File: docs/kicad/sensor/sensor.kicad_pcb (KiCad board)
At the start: 2 copper layers, 30 x 26 mm, 6 parts, among them J1 G 5 L D

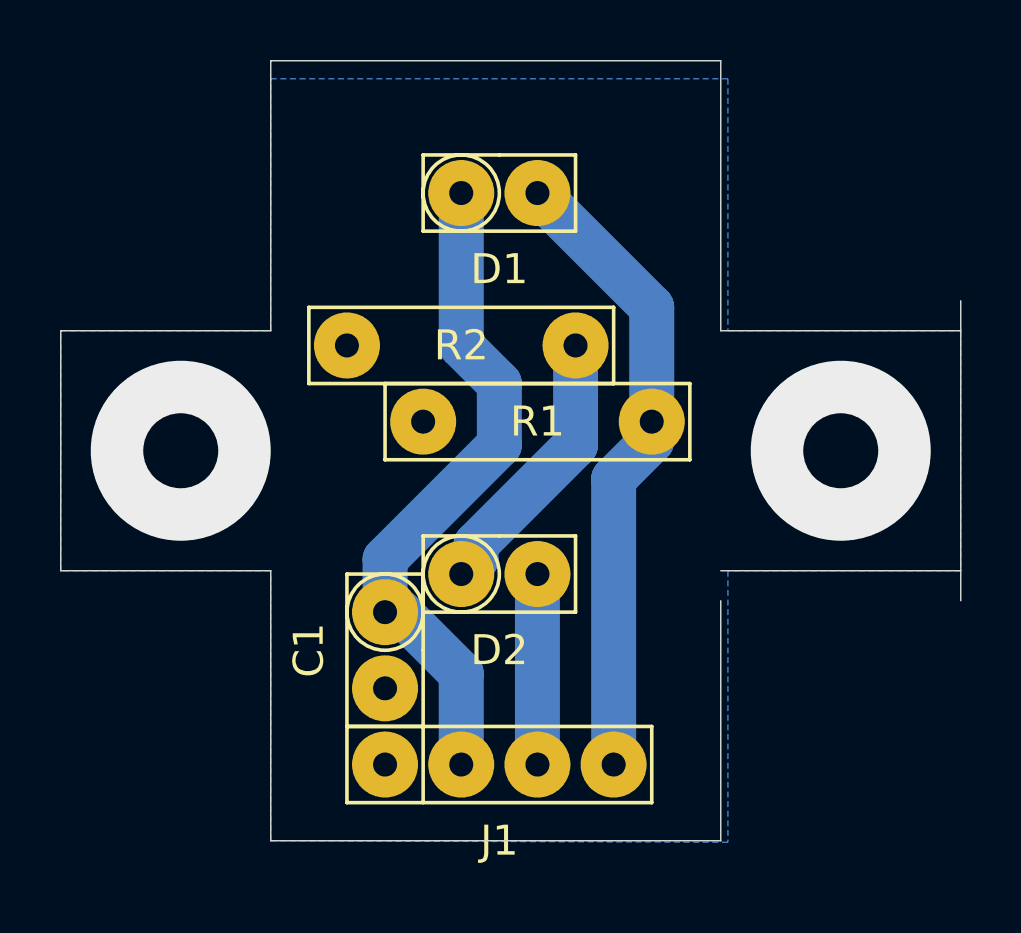
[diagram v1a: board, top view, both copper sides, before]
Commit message: SIMPLIFY: got rid of buttons and compass, smaller PCB, all new outputs
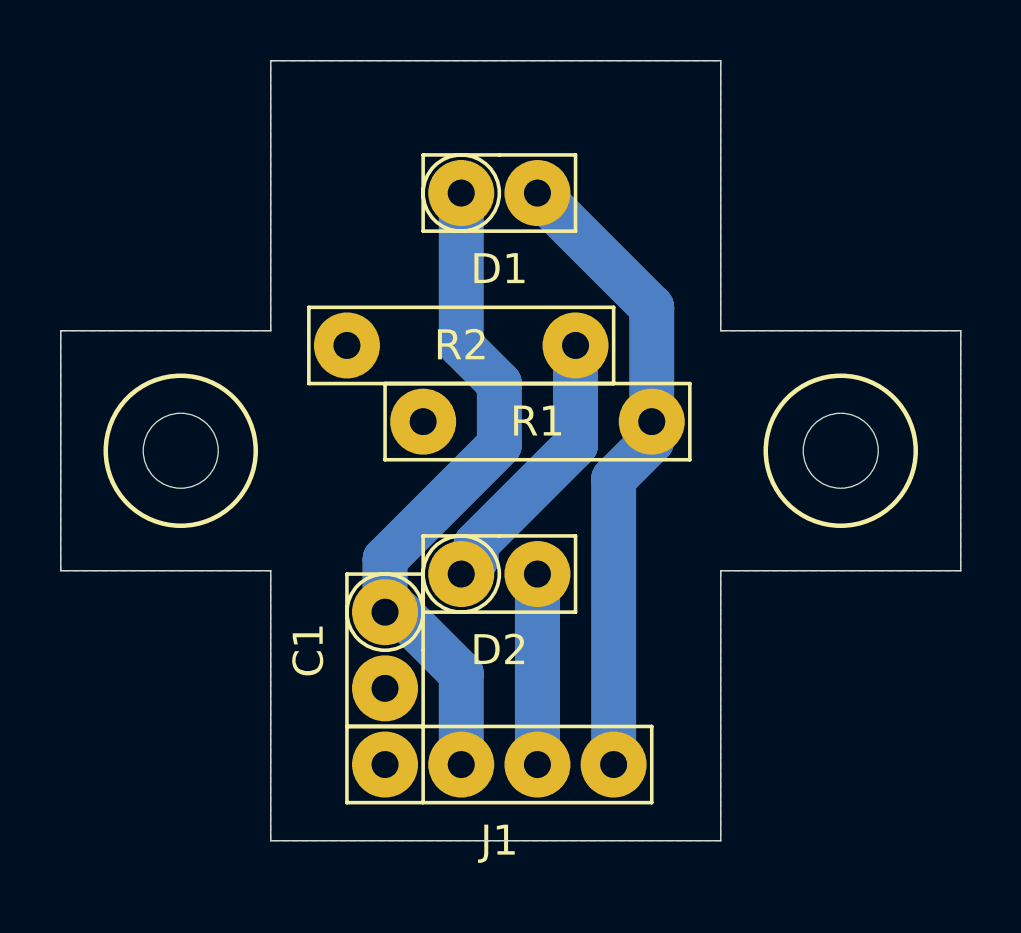
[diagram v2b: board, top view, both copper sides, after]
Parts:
- added REF**: myMountingHole_2.5mm, 0_my_footprints:myMountingHole_2.5mm, F.Cu at (4.00, -13.0)
- added REF**: myMountingHole_2.5mm, 0_my_footprints:myMountingHole_2.5mm, F.Cu at (26.0, -13.0)
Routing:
- net (no net): vias 2 -> 0
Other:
- outline, holes or cut-outs redrawn
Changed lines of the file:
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@@
   (general
     (thickness 1.6)
-    (drawings 24)
-    (tracks 20)
+    (drawings 23)
+    (tracks 18)
     (zones 0)
-    (modules 6)
+    (modules 8)
     (nets 6)
   )
@@
     (mod_text_size 1 1)
     (mod_text_width 0.15)
-    (pad_size 1.524 1.524)
-    (pad_drill 0.762)
+    (pad_size 2.2 2.2)
+    (pad_drill 0.9)
     (pad_to_mask_clearance 0.05)
     (aux_axis_origin 0 0)
@@
     (add_net "Net-(D2-Pad2)")
   )
+  (module 0_my_footprints:myMountingHole_2.5mm (layer F.Cu)
+    (at 4 -13)
+    (descr "Mounting Hole 2.5mm, no annular")
+    (tags "mounting hole 2.5mm no annular")
+    (attr virtual)
+    (fp_text reference REF** (at 0 -3.5) (layer B.Fab)
+      (effects (font (size 1 1) (thickness 0.15)))
+    )
+    (fp_text value myMountingHole_2.5mm (at 0 3.5) (layer B.Fab)
+      (effects (font (size 1 1) (thickness 0.15)))
+    )
+    (fp_circle (center 0 0) (end 2.5 0) (layer F.SilkS) (width 0.15))
+    (pad 1 np_thru_hole circle (at 0 0) (size 2.5 2.5) (drill 2.5) (layers *.Cu *.Mask))
+  )
+  (module 0_my_footprints:myMountingHole_2.5mm (layer F.Cu)
+    (at 26 -13)
+    (descr "Mounting Hole 2.5mm, no annular")
+    (tags "mounting hole 2.5mm no annular")
+    (attr virtual)
+    (fp_text reference REF** (at 0 -3.5) (layer B.Fab)
+      (effects (font (size 1 1) (thickness 0.15)))
+    )
+    (fp_text value myMountingHole_2.5mm (at 0 3.5) (layer B.Fab)
+      (effects (font (size 1 1) (thickness 0.15)))
+    )
+    (fp_circle (center 0 0) (end 2.5 0) (layer F.SilkS) (width 0.15))
+    (pad 1 np_thru_hole circle (at 0 0) (size 2.5 2.5) (drill 2.5) (layers *.Cu *.Mask))
+  )
   (module cnc3018-PCB:my2pin (layer F.Cu)
     (at 10.81 -7.62 270)
@@
     (fp_line (start 3.81 1.27) (end 3.81 -1.27) (layer F.SilkS) (width 0.12))
     (fp_line (start 3.81 -1.27) (end 1.27 -1.27) (layer F.SilkS) (width 0.12))
-    (pad 2 thru_hole circle (at 2.54 0 270) (size 2.2 2.2) (drill 0.8) (layers *.Cu *.Mask)
+    (pad 2 thru_hole circle (at 2.54 0 270) (size 2.2 2.2) (drill 0.9) (layers *.Cu *.Mask)
       (net 5 GND))
-    (pad 1 thru_hole circle (at 0 0 270) (size 2.2 2.2) (drill 0.8) (layers *.Cu *.Mask)
+    (pad 1 thru_hole circle (at 0 0 270) (size 2.2 2.2) (drill 0.9) (layers *.Cu *.Mask)
       (net 4 +5V))
   )
@@
     (fp_line (start -1.27 -1.27) (end 1.27 -1.27) (layer F.SilkS) (width 0.12))
     (fp_line (start -1.27 -1.27) (end -1.27 1.27) (layer F.SilkS) (width 0.12))
-    (pad 1 thru_hole circle (at 0 0) (size 2.2 2.2) (drill 0.8) (layers *.Cu *.Mask)
+    (pad 1 thru_hole circle (at 0 0) (size 2.2 2.2) (drill 0.9) (layers *.Cu *.Mask)
       (net 4 +5V))
-    (pad 2 thru_hole circle (at 2.54 0) (size 2.2 2.2) (drill 0.8) (layers *.Cu *.Mask)
+    (pad 2 thru_hole circle (at 2.54 0) (size 2.2 2.2) (drill 0.9) (layers *.Cu *.Mask)
       (net 1 "Net-(D1-Pad2)"))
   )
@@
     (fp_line (start 3.81 1.27) (end 3.81 -1.27) (layer F.SilkS) (width 0.12))
     (fp_line (start 3.81 -1.27) (end 1.27 -1.27) (layer F.SilkS) (width 0.12))
-    (pad 2 thru_hole circle (at 2.54 0) (size 2.2 2.2) (drill 0.8) (layers *.Cu *.Mask)
+    (pad 2 thru_hole circle (at 2.54 0) (size 2.2 2.2) (drill 0.9) (layers *.Cu *.Mask)
       (net 3 "Net-(D2-Pad2)"))
-    (pad 1 thru_hole circle (at 0 0) (size 2.2 2.2) (drill 0.8) (layers *.Cu *.Mask)
+    (pad 1 thru_hole circle (at 0 0) (size 2.2 2.2) (drill 0.9) (layers *.Cu *.Mask)
       (net 2 "Net-(D2-Pad1)"))
   )
@@
     (fp_line (start 8.89 1.27) (end 8.89 -1.27) (layer F.SilkS) (width 0.12))
     (fp_line (start 8.89 -1.27) (end 1.27 -1.27) (layer F.SilkS) (width 0.12))
-    (pad 4 thru_hole circle (at 7.62 0) (size 2.2 2.2) (drill 0.8) (layers *.Cu *.Mask)
+    (pad 4 thru_hole circle (at 7.62 0) (size 2.2 2.2) (drill 0.9) (layers *.Cu *.Mask)
       (net 1 "Net-(D1-Pad2)"))
-    (pad 3 thru_hole circle (at 5.08 0) (size 2.2 2.2) (drill 0.8) (layers *.Cu *.Mask)
+    (pad 3 thru_hole circle (at 5.08 0) (size 2.2 2.2) (drill 0.9) (layers *.Cu *.Mask)
       (net 3 "Net-(D2-Pad2)"))
-    (pad 2 thru_hole circle (at 2.54 0) (size 2.2 2.2) (drill 0.8) (layers *.Cu *.Mask)
+    (pad 2 thru_hole circle (at 2.54 0) (size 2.2 2.2) (drill 0.9) (layers *.Cu *.Mask)
       (net 4 +5V))
-    (pad 1 thru_hole circle (at 0 0) (size 2.2 2.2) (drill 0.8) (layers *.Cu *.Mask)
+    (pad 1 thru_hole circle (at 0 0) (size 2.2 2.2) (drill 0.9) (layers *.Cu *.Mask)
       (net 5 GND))
   )
@@
     (fp_line (start 8.89 -1.27) (end -1.27 -1.27) (layer F.SilkS) (width 0.12))
     (fp_line (start 8.89 -1.27) (end 8.89 1.27) (layer F.SilkS) (width 0.12))
-    (pad 2 thru_hole circle (at 7.62 0) (size 2.2 2.2) (drill 0.8) (layers *.Cu *.Mask)
+    (pad 2 thru_hole circle (at 7.62 0) (size 2.2 2.2) (drill 0.9) (layers *.Cu *.Mask)
       (net 1 "Net-(D1-Pad2)"))
-    (pad 1 thru_hole circle (at 0 0) (size 2.2 2.2) (drill 0.8) (layers *.Cu *.Mask)
+    (pad 1 thru_hole circle (at 0 0) (size 2.2 2.2) (drill 0.9) (layers *.Cu *.Mask)
       (net 5 GND))
   )
@@
     (fp_line (start -1.27 -1.27) (end -1.27 1.27) (layer F.SilkS) (width 0.12))
     (fp_line (start -1.27 1.27) (end 8.89 1.27) (layer F.SilkS) (width 0.12))
-    (pad 1 thru_hole circle (at 0 0 180) (size 2.2 2.2) (drill 0.8) (layers *.Cu *.Mask)
+    (pad 1 thru_hole circle (at 0 0 180) (size 2.2 2.2) (drill 0.9) (layers *.Cu *.Mask)
       (net 2 "Net-(D2-Pad1)"))
-    (pad 2 thru_hole circle (at 7.62 0 180) (size 2.2 2.2) (drill 0.8) (layers *.Cu *.Mask)
+    (pad 2 thru_hole circle (at 7.62 0 180) (size 2.2 2.2) (drill 0.9) (layers *.Cu *.Mask)
       (net 5 GND))
   )
@@
   (gr_line (start 7 0) (end 7 -9) (layer Edge.Cuts) (width 0.05))
   (gr_line (start 22 0) (end 7 0) (layer Edge.Cuts) (width 0.05))
-  (gr_line (start 22 -8) (end 22 0) (layer Edge.Cuts) (width 0.05))
+  (gr_line (start 22 -9) (end 22 0) (layer Edge.Cuts) (width 0.05))
   (gr_line (start 30 -9) (end 22 -9) (layer Edge.Cuts) (width 0.05))
-  (gr_line (start 30 -18) (end 30 -8) (layer Edge.Cuts) (width 0.05))
+  (gr_line (start 30 -17) (end 30 -9) (layer Edge.Cuts) (width 0.05))
   (gr_line (start 22 -17) (end 30 -17) (layer Edge.Cuts) (width 0.05))
   (gr_line (start 22 -26) (end 22 -17) (layer Edge.Cuts) (width 0.05))
@@
     (arrow2b (pts (xy 4 12) (xy 5.126504 11.413579)))
   )
-  (dimension 15.24 (width 0.15) (layer Dwgs.User)
-    (gr_text "15.240 mm" (at 14.62 6.38) (layer Dwgs.User)
-      (effects (font (size 1 1) (thickness 0.15)))
-    )
-    (feature1 (pts (xy 22.24 0) (xy 22.24 5.666421)))
+  (dimension 15 (width 0.15) (layer Dwgs.User)
+    (gr_text "15.000 mm" (at 14.5 6.38) (layer Dwgs.User)
+      (effects (font (size 1 1) (thickness 0.15)))
+    )
+    (feature1 (pts (xy 22 0) (xy 22 5.666421)))
     (feature2 (pts (xy 7 0) (xy 7 5.666421)))
-    (crossbar (pts (xy 7 5.08) (xy 22.24 5.08)))
-    (arrow1a (pts (xy 22.24 5.08) (xy 21.113496 5.666421)))
-    (arrow1b (pts (xy 22.24 5.08) (xy 21.113496 4.493579)))
+    (crossbar (pts (xy 7 5.08) (xy 22 5.08)))
+    (arrow1a (pts (xy 22 5.08) (xy 20.873496 5.666421)))
+    (arrow1b (pts (xy 22 5.08) (xy 20.873496 4.493579)))
     (arrow2a (pts (xy 7 5.08) (xy 8.126504 5.666421)))
     (arrow2b (pts (xy 7 5.08) (xy 8.126504 4.493579)))
   )
-  (dimension 25.4 (width 0.15) (layer Dwgs.User)
-    (gr_text "25.400 mm" (at 37.3 -12.7 270) (layer Dwgs.User)
-      (effects (font (size 1 1) (thickness 0.15)))
-    )
-    (feature1 (pts (xy 22.24 0) (xy 36.586421 0)))
-    (feature2 (pts (xy 22.24 -25.4) (xy 36.586421 -25.4)))
-    (crossbar (pts (xy 36 -25.4) (xy 36 0)))
-    (arrow1a (pts (xy 36 0) (xy 35.413579 -1.126504)))
-    (arrow1b (pts (xy 36 0) (xy 36.586421 -1.126504)))
-    (arrow2a (pts (xy 36 -25.4) (xy 35.413579 -24.273496)))
-    (arrow2b (pts (xy 36 -25.4) (xy 36.586421 -24.273496)))
-  )
-  (via (at 4 -13) (size 6) (drill 2.5) (layers F.Cu B.Cu) (net 0))
-  (via (at 26 -13) (size 6) (drill 2.5) (layers F.Cu B.Cu) (net 0))
   (segment (start 19.7 -13.329825) (end 19.7 -13.97) (width 1.5) (layer B.Cu) (net 1))
   (segment (start 18.43 -12.059825) (end 19.7 -13.329825) (width 1.5) (layer B.Cu) (net 1))
@@
     (polygon
       (pts
-        (xy 22.24 -17) (xy 30 -17) (xy 30 -9) (xy 22.24 -9) (xy 22.24 0.05)
+        (xy 22 -17) (xy 30 -17) (xy 30 -9) (xy 22 -9) (xy 22 0)
         (xy 7 0) (xy 7 -9) (xy 0 -9) (xy 0 -17) (xy 7 -17)
-        (xy 7 -25.4) (xy 22.24 -25.4)
+        (xy 7 -26) (xy 22 -26)
       )
     )
